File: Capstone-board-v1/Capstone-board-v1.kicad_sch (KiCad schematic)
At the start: 22 parts, among them J1 Pico Socket 1, J2 Pico Socket 2, M1 DC Vibration Motor, Q1 2N3904, U1 3.3 V Voltage Regulator, U2 555 Timer, U3 Gyroscope Sensor, U4 OP-Amp, U5 Hall Effect Sensor

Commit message: ready for tracing
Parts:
- BT1: footprint (none) -> Battery:Battery_Panasonic_CR1025-VSK_Vertical_CircularHoles
- C1, C2, C3: footprint (none) -> Capacitor_THT:CP_Axial_L10.0mm_D4.5mm_P15.00mm_Horizontal
- M1: footprint (none) -> Connector_PinHeader_1.27mm:PinHeader_1x02_P1.27mm_Vertical
- R1, R2, R3, R4, R5, R6: footprint (none) -> Resistor_THT:R_Axial_DIN0204_L3.6mm_D1.6mm_P5.08mm_Horizontal
- U4: footprint (none) -> Package_DIP:DIP-8_W7.62mm_Socket
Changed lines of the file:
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@@
       (effects (font (size 1.27 1.27)) (justify right))
     )
-    (property "Footprint" "" (at 80.264 100.076 90)
+    (property "Footprint" "Resistor_THT:R_Axial_DIN0204_L3.6mm_D1.6mm_P5.08mm_Horizontal" (at 80.264 100.076 90)
       (effects (font (size 1.27 1.27)) hide)
     )
@@
       (effects (font (size 1.27 1.27)) (justify left))
     )
-    (property "Footprint" "" (at 40.64 50.546 90)
+    (property "Footprint" "Battery:Battery_Panasonic_CR1025-VSK_Vertical_CircularHoles" (at 40.64 50.546 90)
       (effects (font (size 1.27 1.27)) hide)
     )
@@
       (effects (font (size 1.27 1.27)) (justify right))
     )
-    (property "Footprint" "" (at 80.264 89.916 90)
+    (property "Footprint" "Resistor_THT:R_Axial_DIN0204_L3.6mm_D1.6mm_P5.08mm_Horizontal" (at 80.264 89.916 90)
       (effects (font (size 1.27 1.27)) hide)
     )
@@
       (effects (font (size 1.27 1.27)))
     )
-    (property "Footprint" "" (at 96.266 121.666 90)
+    (property "Footprint" "Resistor_THT:R_Axial_DIN0204_L3.6mm_D1.6mm_P5.08mm_Horizontal" (at 96.266 121.666 90)
       (effects (font (size 1.27 1.27)) hide)
     )
@@
       (effects (font (size 1.27 1.27)))
     )
-    (property "Footprint" "" (at 86.614 82.804 90)
+    (property "Footprint" "Resistor_THT:R_Axial_DIN0204_L3.6mm_D1.6mm_P5.08mm_Horizontal" (at 86.614 82.804 90)
       (effects (font (size 1.27 1.27)) hide)
     )
@@
       (effects (font (size 1.27 1.27)))
     )
-    (property "Footprint" "" (at 101.346 175.006 90)
+    (property "Footprint" "Resistor_THT:R_Axial_DIN0204_L3.6mm_D1.6mm_P5.08mm_Horizontal" (at 101.346 175.006 90)
       (effects (font (size 1.27 1.27)) hide)
     )
@@
       (effects (font (size 1.27 1.27)) (justify left))
     )
-    (property "Footprint" "" (at 111.4552 109.22 0)
+    (property "Footprint" "Capacitor_THT:CP_Axial_L10.0mm_D4.5mm_P15.00mm_Horizontal" (at 111.4552 109.22 0)
       (effects (font (size 1.27 1.27)) hide)
     )
@@
       (effects (font (size 1.27 1.27)) (justify left))
     )
-    (property "Footprint" "" (at 88.646 180.594 90)
+    (property "Footprint" "Resistor_THT:R_Axial_DIN0204_L3.6mm_D1.6mm_P5.08mm_Horizontal" (at 88.646 180.594 90)
       (effects (font (size 1.27 1.27)) hide)
     )
@@
       (effects (font (size 1.27 1.27)))
     )
-    (property "Footprint" "" (at 100.33 160.02 0)
+    (property "Footprint" "Package_DIP:DIP-8_W7.62mm_Socket" (at 100.33 160.02 0)
       (effects (font (size 1.27 1.27)) hide)
     )
@@
       (effects (font (size 1.27 1.27)) (justify left))
     )
-    (property "Footprint" "" (at 133.35 114.046 0)
+    (property "Footprint" "Connector_PinHeader_1.27mm:PinHeader_1x02_P1.27mm_Vertical" (at 133.35 114.046 0)
       (effects (font (size 1.27 1.27)) hide)
     )
@@
       (effects (font (size 1.27 1.27)) (justify left))
     )
-    (property "Footprint" "" (at 139.3952 77.47 0)
+    (property "Footprint" "Capacitor_THT:CP_Axial_L10.0mm_D4.5mm_P15.00mm_Horizontal" (at 139.3952 77.47 0)
       (effects (font (size 1.27 1.27)) hide)
     )
@@
       (effects (font (size 1.27 1.27)) (justify left))
     )
-    (property "Footprint" "" (at 45.4152 95.25 0)
-      (effects (font (size 1.27 1.27)) hide)
-    )
+    (property "Footprint" "Capacitor_THT:CP_Axial_L10.0mm_D4.5mm_P15.00mm_Horizontal" (at 45.4152 95.25 0)
+      (effects (font (size 1.27 1.27)) hide)
+    )

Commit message: correct hole size
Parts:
- C1, C2, C3: footprint Capacitor_THT:CP_Axial_L10.0mm_D4.5mm_P15.00mm_Horizontal -> Capacitor_THT:CP_Radial_Tantal_D4.5mm_P5.00mm
- J1, J2: footprint Connector_PinSocket_1.00mm:PinSocket_1x20_P1.00mm_Vertical -> Connector_PinSocket_2.54mm:PinSocket_1x20_P2.54mm_Vertical
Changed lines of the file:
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@@
       (effects (font (size 1.27 1.27)) (justify left))
     )
-    (property "Footprint" "Capacitor_THT:CP_Axial_L10.0mm_D4.5mm_P15.00mm_Horizontal" (at 111.4552 109.22 0)
+    (property "Footprint" "Capacitor_THT:CP_Radial_Tantal_D4.5mm_P5.00mm" (at 111.4552 109.22 0)
       (effects (font (size 1.27 1.27)) hide)
     )
@@
       (effects (font (size 1.27 1.27)) (justify left))
     )
-    (property "Footprint" "Connector_PinSocket_1.00mm:PinSocket_1x20_P1.00mm_Vertical" (at 229.87 76.2 0)
+    (property "Footprint" "Connector_PinSocket_2.54mm:PinSocket_1x20_P2.54mm_Vertical" (at 229.87 76.2 0)
       (effects (font (size 1.27 1.27)) hide)
     )
@@
       (effects (font (size 1.27 1.27)))
     )
-    (property "Footprint" "Connector_PinSocket_1.00mm:PinSocket_1x20_P1.00mm_Vertical" (at 247.65 78.74 0)
+    (property "Footprint" "Connector_PinSocket_2.54mm:PinSocket_1x20_P2.54mm_Vertical" (at 247.65 78.74 0)
       (effects (font (size 1.27 1.27)) hide)
     )
@@
       (effects (font (size 1.27 1.27)) (justify left))
     )
-    (property "Footprint" "Capacitor_THT:CP_Axial_L10.0mm_D4.5mm_P15.00mm_Horizontal" (at 139.3952 77.47 0)
+    (property "Footprint" "Capacitor_THT:CP_Radial_Tantal_D4.5mm_P5.00mm" (at 139.3952 77.47 0)
       (effects (font (size 1.27 1.27)) hide)
     )
@@
       (effects (font (size 1.27 1.27)) (justify left))
     )
-    (property "Footprint" "Capacitor_THT:CP_Axial_L10.0mm_D4.5mm_P15.00mm_Horizontal" (at 45.4152 95.25 0)
-      (effects (font (size 1.27 1.27)) hide)
-    )
+    (property "Footprint" "Capacitor_THT:CP_Radial_Tantal_D4.5mm_P5.00mm" (at 45.4152 95.25 0)
+      (effects (font (size 1.27 1.27)) hide)
+    )

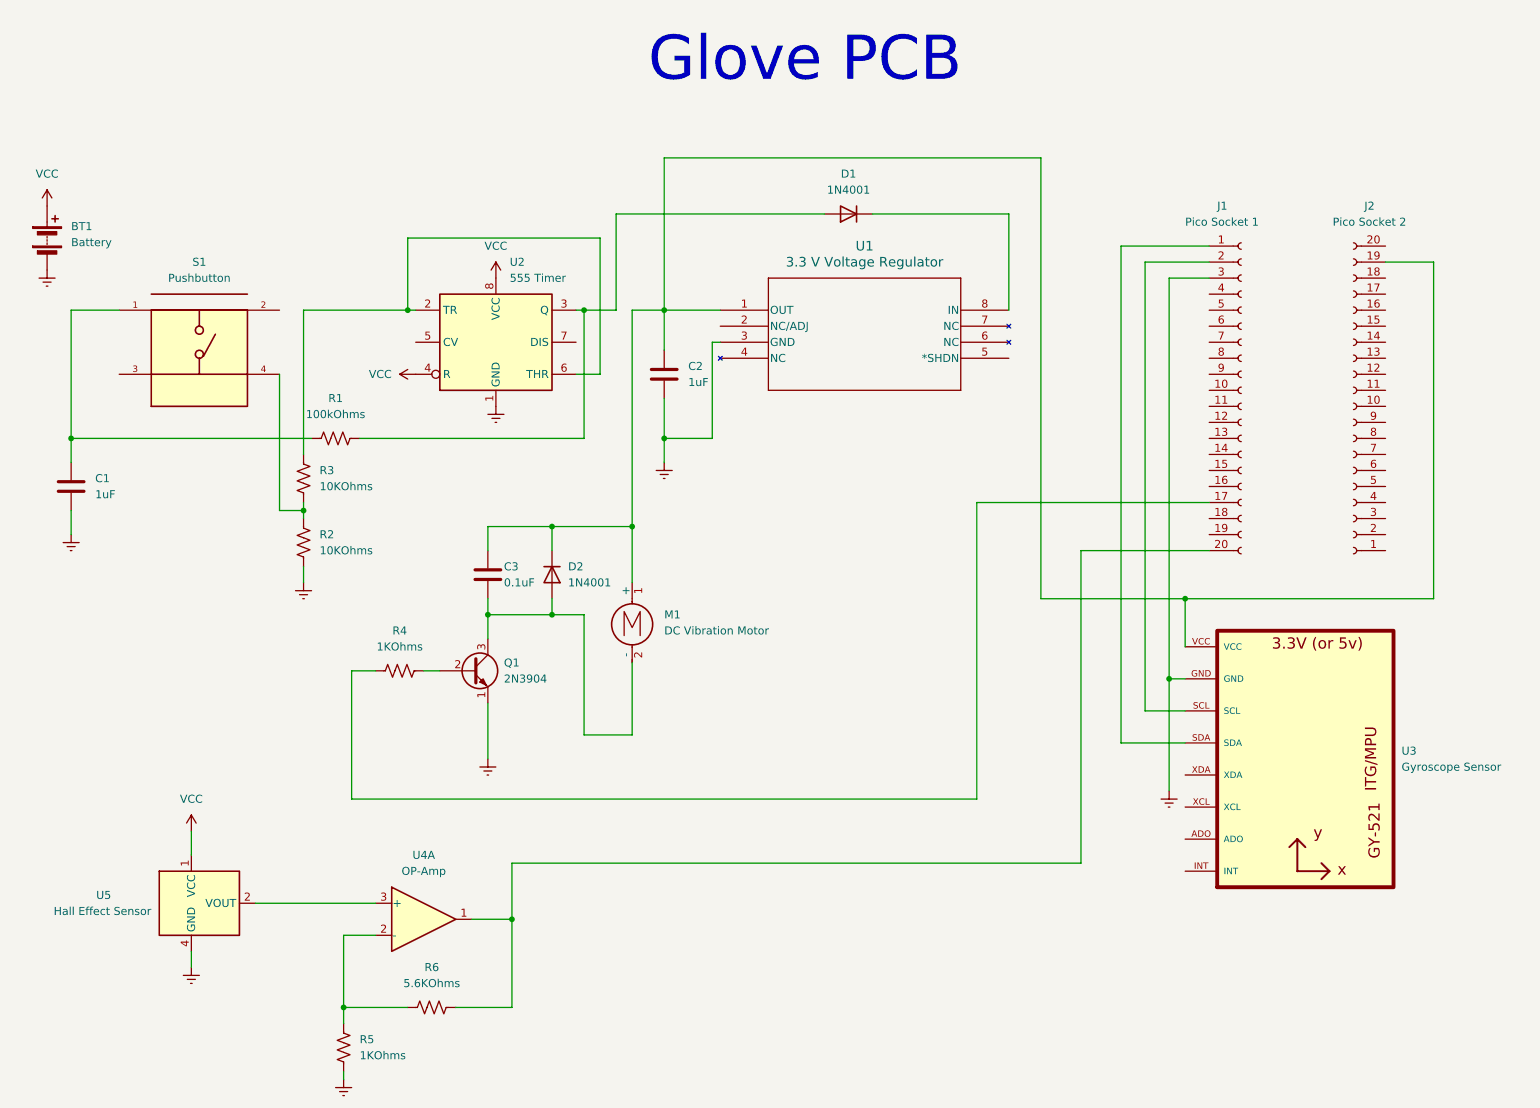
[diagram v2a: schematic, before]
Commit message: traces added
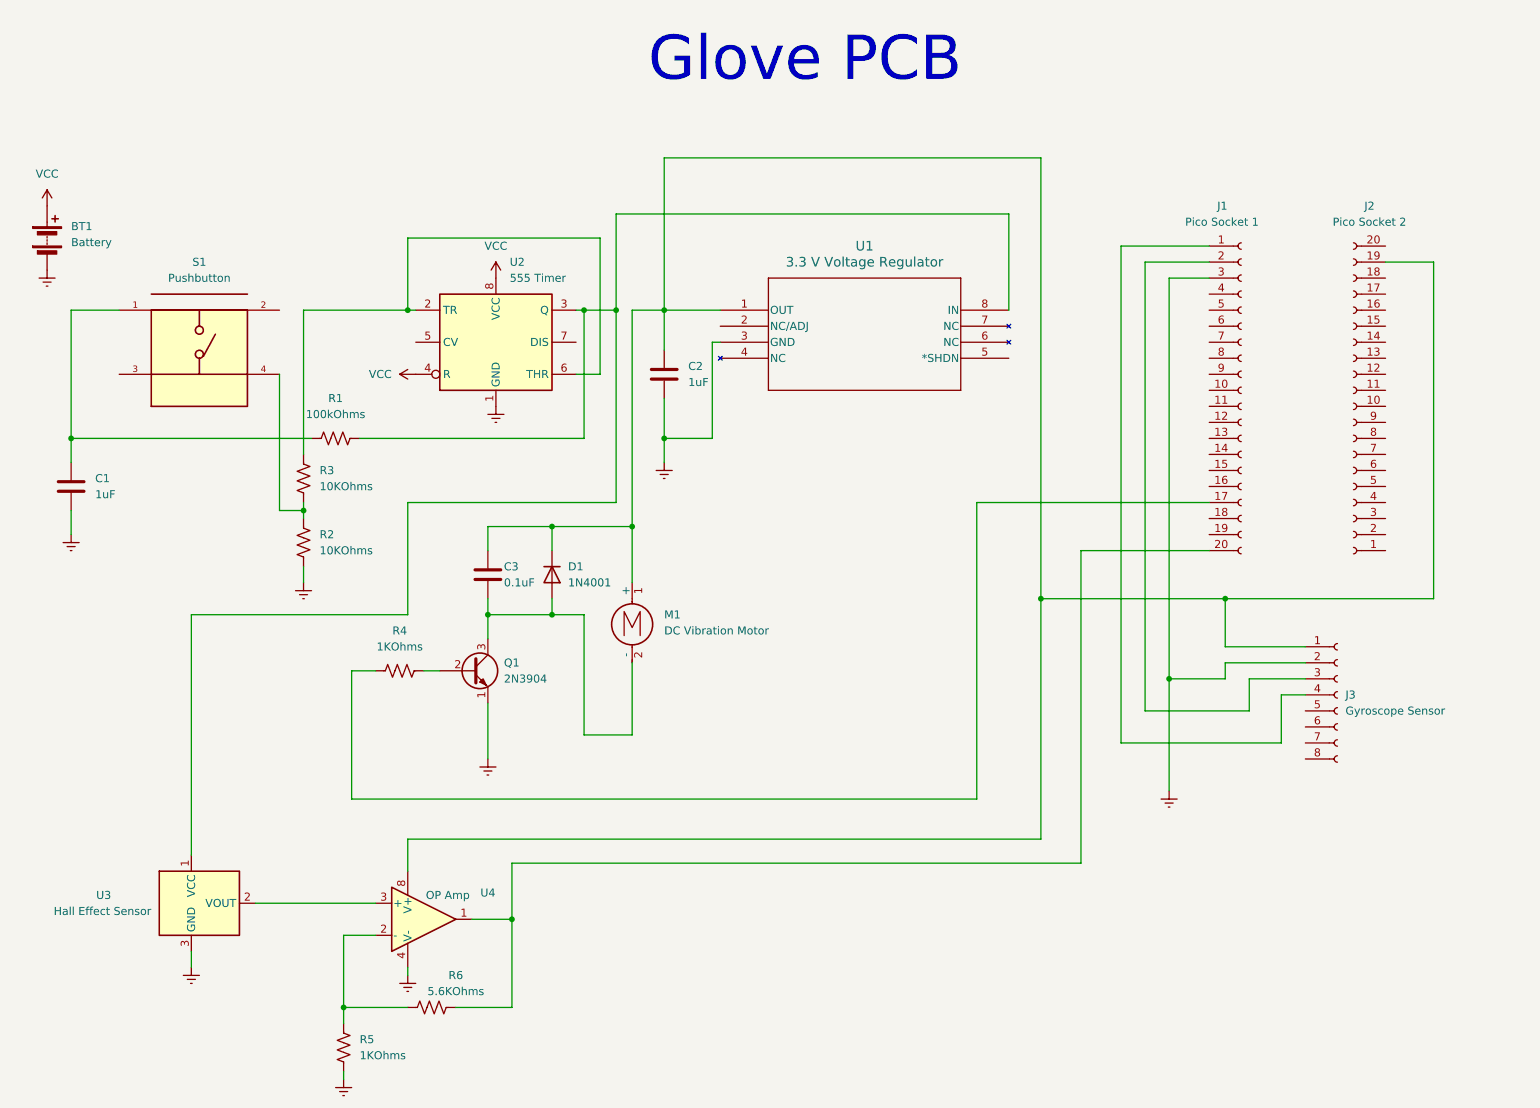
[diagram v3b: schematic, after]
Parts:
- removed D1: 1N4001, Diode_THT:D_DO-41_SOD81_P10.16mm_Horizontal, symbol Diode:1N4001
- removed U3: Gyroscope Sensor, GY-521:GY-521, symbol GY-521:GY-521
- removed U4: OP-Amp, Package_DIP:DIP-8_W7.62mm_Socket, symbol Amplifier_Operational:TLV2372
- added J3: Gyroscope Sensor, Connector_PinSocket_2.54mm:PinSocket_1x08_P2.54mm_Vertical, symbol Connector:Conn_01x08_Socket
- added U4: OP Amp, Package_DIP:DIP-8_W7.62mm_Socket, symbol Simulation_SPICE:OPAMP
- BT1: footprint Battery:Battery_Panasonic_CR1025-VSK_Vertical_CircularHoles -> Connector_Hirose:Hirose_DF11-4DP-2DSA_2x02_P2.00mm_Vertical
- M1: footprint Connector_PinHeader_1.27mm:PinHeader_1x02_P1.27mm_Vertical -> Connector_Hirose:Hirose_DF13-02P-1.25DSA_1x02_P1.25mm_Vertical
- S1: footprint TS02-66-60-BK-100-LCR-D:SW_TS02-66-60-BK-160-LCR-D -> TS:SW_TS02-66-60-BK-160-LCR-D
- U1, U2: footprint Package_DIP:DIP-8_W7.62mm -> Package_DIP:DIP-8_W7.62mm_Socket
- U3: renamed from U5; footprint Sensor_Current:Allegro_SIP-4 -> Connector_Hirose:Hirose_DF13-03P-1.25DSA_1x03_P1.25mm_Vertical
- renumbered D2 to D1
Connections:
- net Earth: now also U3.3 (NC), J3.2 (Pin_2), U4.4 (V-); no longer U3.4 (GND)
- net VCC: no longer U3.1 (VCC)
- net at R1.2, U2.3 (Q): now also U1.8 (IN), U3.1 (VCC)
- net at J1.2 (Pin_2): now also J3.3 (Pin_3)
- net at J1.1 (Pin_1): now also J3.4 (Pin_4)
- net at C2.1, C3.1, D1.1 (K)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: now also J3.1 (Pin_1), U4.8 (V+)
- net at J1.20 (Pin_20), R6.1: now also U4.1
- net at R5.1, R6.2: now also U4.2 (-)
- net at U3.2 (VOUT): now also U4.3 (+)

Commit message: Final traces done
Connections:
- net VCC: now also R3.2
- net at U2.2 (TR), U2.6 (THR): now also R2.2, R3.1, S1.4; no longer R3.2
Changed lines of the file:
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@@
   (junction (at 218.44 121.92) (diameter 0) (color 0 0 0 0)
   )
+  (junction (at 124.46 73.66) (diameter 0) (color 0 0 0 0)
+  )
   (junction (at 44.45 83.82) (diameter 0) (color 0 0 0 0)
   )
@@
   (junction (at 120.65 111.76) (diameter 0) (color 0 0 0 0)
   )
-  (junction (at 97.79 63.5) (diameter 0) (color 0 0 0 0)
-  )
   (junction (at 114.3 160.02) (diameter 0) (color 0 0 0 0)
   )
@@
     (stroke (width 0) (type default))
   )
+  (wire (pts (xy 124.46 73.66) (xy 128.27 73.66))
+    (stroke (width 0) (type default))
+  )
   (wire (pts (xy 81.28 95.25) (xy 81.28 96.52))
     (stroke (width 0) (type default))
   )
+  (wire (pts (xy 124.46 90.17) (xy 93.98 90.17))
+    (stroke (width 0) (type default))
+  )
   (wire (pts (xy 204.47 101.6) (xy 204.47 151.13))
     (stroke (width 0) (type default))
@@
     (stroke (width 0) (type default))
   )
-  (wire (pts (xy 128.27 73.66) (xy 124.46 73.66))
-    (stroke (width 0) (type default))
-  )
   (wire (pts (xy 110.49 111.76) (xy 110.49 115.57))
     (stroke (width 0) (type default))
@@
     (stroke (width 0) (type default))
   )
+  (wire (pts (xy 81.28 73.66) (xy 81.28 86.36))
+    (stroke (width 0) (type default))
+  )
   (wire (pts (xy 128.27 52.07) (xy 128.27 73.66))
     (stroke (width 0) (type default))
@@
     (stroke (width 0) (type default))
   )
+  (wire (pts (xy 124.46 73.66) (xy 124.46 90.17))
+    (stroke (width 0) (type default))
+  )
   (wire (pts (xy 125.73 111.76) (xy 120.65 111.76))
     (stroke (width 0) (type default))
@@
     (stroke (width 0) (type default))
   )
-  (wire (pts (xy 81.28 86.36) (xy 81.28 63.5))
-    (stroke (width 0) (type default))
-  )
   (wire (pts (xy 133.35 97.79) (xy 133.35 63.5))
     (stroke (width 0) (type default))
@@
     (stroke (width 0) (type default))
   )
+  (wire (pts (xy 81.28 95.25) (xy 93.98 95.25))
+    (stroke (width 0) (type default))
+  )
   (wire (pts (xy 87.63 173.99) (xy 87.63 176.53))
     (stroke (width 0) (type default))
   )
-  (wire (pts (xy 81.28 63.5) (xy 97.79 63.5))
-    (stroke (width 0) (type default))
-  )
   (wire (pts (xy 114.3 160.02) (xy 114.3 173.99))
     (stroke (width 0) (type default))
@@
   )
   (wire (pts (xy 187.96 140.97) (xy 187.96 93.98))
+    (stroke (width 0) (type default))
+  )
+  (wire (pts (xy 93.98 90.17) (xy 93.98 95.25))
     (stroke (width 0) (type default))
   )
@@
         )
       )
+    )
+  )
+  (symbol (lib_id "power:VCC") (at 81.28 73.66 0) (unit 1)
+    (in_bom yes) (on_board yes) (dnp no) (fields_autoplaced)
+    (property "Reference" "#PWR014" (at 81.28 77.47 0)
+      (effects (font (size 1.27 1.27)) hide)
+    )
+    (property "Value" "VCC" (at 81.28 68.58 0)
+      (effects (font (size 1.27 1.27)))
+    )
+    (property "Footprint" "" (at 81.28 73.66 0)
+      (effects (font (size 1.27 1.27)) hide)
+    )
+    (property "Datasheet" "" (at 81.28 73.66 0)
+      (effects (font (size 1.27 1.27)) hide)
+    )
+    (pin "1")
+    (instances
+      (project "Capstone-board-v1"
+        (path "/5a0b0107-0183-4094-a3d7-2a417dfae25a"
+          (reference "#PWR014") (unit 1)
+        )
+      )

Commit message: Final PCB completed!
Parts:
- U1: value 3.3 V Voltage Regulator -> 3.3 V V.R
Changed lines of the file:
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@@
       (effects (font (size 1.524 1.524)))
     )
-    (property "Value" "3.3 V Voltage Regulator" (at 170.18 55.88 0)
+    (property "Value" "3.3 V V.R" (at 170.18 55.88 0)
       (effects (font (size 1.524 1.524)))
     )

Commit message: Final PCBs done!
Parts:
- BT1: footprint Connector_Hirose:Hirose_DF11-4DP-2DSA_2x02_P2.00mm_Vertical -> Connector_Hirose:Hirose_DF11-6DP-2DSA_2x03_P2.00mm_Vertical
- M1: footprint Connector_Hirose:Hirose_DF13-02P-1.25DSA_1x02_P1.25mm_Vertical -> Connector_PinSocket_2.54mm:PinSocket_1x02_P2.54mm_Vertical
- U3: footprint Connector_Hirose:Hirose_DF13-03P-1.25DSA_1x03_P1.25mm_Vertical -> Connector_PinSocket_2.54mm:PinSocket_1x03_P2.54mm_Vertical
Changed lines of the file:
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@@
       (effects (font (size 1.27 1.27)) (justify left))
     )
-    (property "Footprint" "Connector_Hirose:Hirose_DF11-4DP-2DSA_2x02_P2.00mm_Vertical" (at 40.64 50.546 90)
+    (property "Footprint" "Connector_Hirose:Hirose_DF11-6DP-2DSA_2x03_P2.00mm_Vertical" (at 40.64 50.546 90)
       (effects (font (size 1.27 1.27)) hide)
     )
@@
       (effects (font (size 1.27 1.27)) (justify left))
     )
-    (property "Footprint" "Connector_Hirose:Hirose_DF13-02P-1.25DSA_1x02_P1.25mm_Vertical" (at 133.35 114.046 0)
+    (property "Footprint" "Connector_PinSocket_2.54mm:PinSocket_1x02_P2.54mm_Vertical" (at 133.35 114.046 0)
       (effects (font (size 1.27 1.27)) hide)
     )
@@
       (effects (font (size 1.27 1.27)) (justify right))
     )
-    (property "Footprint" "Connector_Hirose:Hirose_DF13-03P-1.25DSA_1x03_P1.25mm_Vertical" (at 72.39 160.02 0)
+    (property "Footprint" "Connector_PinSocket_2.54mm:PinSocket_1x03_P2.54mm_Vertical" (at 72.39 160.02 0)
       (effects (font (size 1.27 1.27) italic) (justify left) hide)
     )
